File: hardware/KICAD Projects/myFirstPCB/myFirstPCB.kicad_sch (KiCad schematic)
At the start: 3 parts

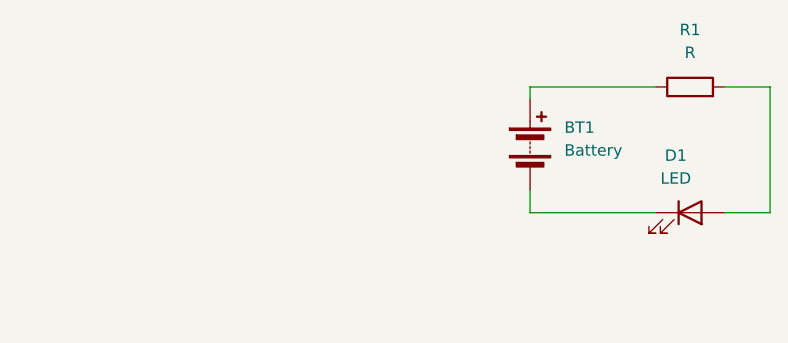
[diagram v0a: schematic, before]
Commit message: ESP 32 S3 Schematic
Completed symbol layout for esp 32
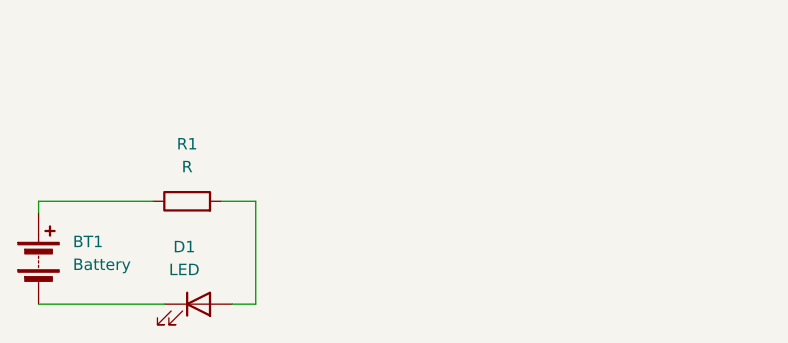
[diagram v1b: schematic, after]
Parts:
- R1: footprint Resistor_THT:R_Axial_DIN0204_L3.6mm_D1.6mm_P5.08mm_Horizontal -> Capacitor_SMD:C_Trimmer_Voltronics_JV
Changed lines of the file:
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@@
 	(wire
 		(pts
-			(xy 127 96.52) (xy 127 93.98)
-		)
-		(stroke
-			(width 0)
-			(type default)
-		)
-	)
-	(wire
-		(pts
-			(xy 153.67 96.52) (xy 148.59 96.52)
-		)
-		(stroke
-			(width 0)
-			(type default)
-		)
-	)
-	(wire
-		(pts
-			(xy 153.67 82.55) (xy 148.59 82.55)
-		)
-		(stroke
-			(width 0)
-			(type default)
-		)
-	)
-	(wire
-		(pts
-			(xy 140.97 96.52) (xy 127 96.52)
-		)
-		(stroke
-			(width 0)
-			(type default)
-		)
-	)
-	(wire
-		(pts
-			(xy 127 82.55) (xy 140.97 82.55)
-		)
-		(stroke
-			(width 0)
-			(type default)
-		)
-	)
-	(wire
-		(pts
-			(xy 127 82.55) (xy 127 83.82)
-		)
-		(stroke
-			(width 0)
-			(type default)
-		)
-	)
-	(wire
-		(pts
-			(xy 153.67 82.55) (xy 153.67 96.52)
+			(xy 96.52 95.25) (xy 96.52 106.68)
+		)
+		(stroke
+			(width 0)
+			(type default)
+		)
+	)
+	(wire
+		(pts
+			(xy 72.39 106.68) (xy 86.36 106.68)
+		)
+		(stroke
+			(width 0)
+			(type default)
+		)
+	)
+	(wire
+		(pts
+			(xy 96.52 95.25) (xy 92.71 95.25)
+		)
+		(stroke
+			(width 0)
+			(type default)
+		)
+	)
+	(wire
+		(pts
+			(xy 72.39 95.25) (xy 85.09 95.25)
+		)
+		(stroke
+			(width 0)
+			(type default)
+		)
+	)
+	(wire
+		(pts
+			(xy 96.52 106.68) (xy 93.98 106.68)
+		)
+		(stroke
+			(width 0)
+			(type default)
+		)
+	)
+	(wire
+		(pts
+			(xy 72.39 95.25) (xy 72.39 96.52)
 		)
 		(stroke
@@
 	(symbol
 		(lib_id "Device:Battery")
-		(at 127 88.9 0)
+		(at 72.39 101.6 0)
 		(unit 1)
 		(exclude_from_sim no)
@@
 		(fields_autoplaced yes)
 		(property "Reference" "BT1"
-			(at 130.81 87.0584 0)
+			(at 76.2 99.7584 0)
 			(effects
 				(font
@@
 		)
 		(property "Value" "Battery"
-			(at 130.81 89.5984 0)
+			(at 76.2 102.2984 0)
 			(effects
 				(font
@@
 		)
 		(property "Footprint" "Battery:Battery_Panasonic_CR2032-HFN_Horizontal_CircularHoles"
-			(at 127 87.376 90)
+			(at 72.39 100.076 90)
 			(effects
 				(font
@@
 		)
 		(property "Datasheet" "~"
-			(at 127 87.376 90)
+			(at 72.39 100.076 90)
 			(effects
 				(font
@@
 		)
 		(property "Description" "Multiple-cell battery"
-			(at 127 88.9 0)
+			(at 72.39 101.6 0)
 			(effects
 				(font
@@
 		(instances
 			(project ""
-				(path "/f3862278-dbaa-4915-863f-979ed2d84b86"
+				(path "/61fae62f-fe9f-4a24-bcc0-8c246aaffd86"
 					(reference "BT1")
 					(unit 1)
@@
 	)
 	(symbol
+		(lib_id "Device:LED")
+		(at 90.17 106.68 0)
+		(unit 1)
+		(exclude_from_sim no)
+		(in_bom yes)
+		(on_board yes)
+		(dnp no)
+		(fields_autoplaced yes)
+		(property "Reference" "D1"
+			(at 88.5825 100.33 0)
+			(effects
+				(font
+					(size 1.27 1.27)
+				)
+			)
+		)
+		(property "Value" "LED"
+			(at 88.5825 102.87 0)
+			(effects
+				(font
+					(size 1.27 1.27)
+				)
+			)
+		)
+		(property "Footprint" "LED_THT:LED_D5.0mm"
+			(at 90.17 106.68 0)
+			(effects
+				(font
+					(size 1.27 1.27)
+				)
+				(hide yes)
+			)
+		)
+		(property "Datasheet" "~"
+			(at 90.17 106.68 0)
+			(effects
+				(font
+					(size 1.27 1.27)
+				)
+				(hide yes)
+			)
+		)
+		(property "Description" "Light emitting diode"
+			(at 90.17 106.68 0)
+			(effects
+				(font
+					(size 1.27 1.27)
+				)
+				(hide yes)
+			)
+		)
+		(property "Sim.Pins" "1=K 2=A"
+			(at 90.17 106.68 0)
+			(effects
+				(font
+					(size 1.27 1.27)
+				)
+				(hide yes)
+			)
+		)
+		(pin "2"
+		)
+		(pin "1"
+		)
+		(instances
+			(project ""
+				(path "/61fae62f-fe9f-4a24-bcc0-8c246aaffd86"
+					(reference "D1")
+					(unit 1)
+				)
+			)
+		)
+	)
+	(symbol
 		(lib_id "Device:R")
-		(at 144.78 82.55 90)
+		(at 88.9 95.25 90)
 		(unit 1)
 		(exclude_from_sim no)
@@
 		(fields_autoplaced yes)
 		(property "Reference" "R1"
-			(at 144.78 76.2 90)
+			(at 88.9 88.9 90)
 			(effects
 				(font
@@
 		)
 		(property "Value" "R"
-			(at 144.78 78.74 90)
-			(effects
-				(font
-					(size 1.27 1.27)
-				)
-			)
-		)
-		(property "Footprint" "Resistor_THT:R_Axial_DIN0204_L3.6mm_D1.6mm_P5.08mm_Horizontal"
-			(at 144.78 84.328 90)
+			(at 88.9 91.44 90)
+			(effects
+				(font
+					(size 1.27 1.27)
+				)
+			)
+		)
+		(property "Footprint" "Capacitor_SMD:C_Trimmer_Voltronics_JV"
+			(at 88.9 97.028 90)
 			(effects
 				(font
@@
 		)
 		(property "Datasheet" "~"
-			(at 144.78 82.55 0)
+			(at 88.9 95.25 0)
 			(effects
 				(font
@@
 		)
 		(property "Description" "Resistor"
-			(at 144.78 82.55 0)
+			(at 88.9 95.25 0)
 			(effects
 				(font
@@
 		(instances
 			(project ""
-				(path "/f3862278-dbaa-4915-863f-979ed2d84b86"
+				(path "/61fae62f-fe9f-4a24-bcc0-8c246aaffd86"
 					(reference "R1")
 					(unit 1)
 				)
-			)
-		)
-	)
-	(symbol
-		(lib_id "Device:LED")
-		(at 144.78 96.52 0)
-		(unit 1)
-		(exclude_from_sim no)
-		(in_bom yes)
-		(on_board yes)
-		(dnp no)
-		(fields_autoplaced yes)
-		(property "Reference" "D1"
-			(at 143.1925 90.17 0)
-			(effects
-				(font
-					(size 1.27 1.27)
-				)
-			)
-		)
-		(property "Value" "LED"
-			(at 143.1925 92.71 0)
-			(effects
-				(font
-					(size 1.27 1.27)
-				)
-			)
-		)
-		(property "Footprint" "LED_THT:LED_D5.0mm"
-			(at 144.78 96.52 0)
-			(effects
-				(font
-					(size 1.27 1.27)
-				)
-				(hide yes)
-			)
-		)
-		(property "Datasheet" "~"
-			(at 144.78 96.52 0)
-			(effects
-				(font
-					(size 1.27 1.27)
-				)
-				(hide yes)
-			)
-		)
-		(property "Description" "Light emitting diode"
-			(at 144.78 96.52 0)
-			(effects
-				(font
-					(size 1.27 1.27)
-				)
-				(hide yes)
-			)
-		)
-		(property "Sim.Pins" "1=K 2=A"
-			(at 144.78 96.52 0)
-			(effects
-				(font
-					(size 1.27 1.27)
-				)
-				(hide yes)
-			)
-		)
-		(pin "2"
-		)
-		(pin "1"
-		)
-		(instances
-			(project ""
-				(path "/f3862278-dbaa-4915-863f-979ed2d84b86"
-					(reference "D1")
-					(unit 1)
-				)
